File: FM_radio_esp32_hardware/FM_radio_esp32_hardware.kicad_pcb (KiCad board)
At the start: 2 copper layers, 85 x 117 mm, 47 parts, among them J1 AudioJack2_Ground_SwitchT, J2 Conn_01x06, J3 Conn_02x03_Odd_Even, J4 Conn_02x03_Odd_Even, SW1 SW_Push, SW2 SW_SPDT, SW3 SW_SPST, U1 ESP32-WROOM-32D, U2 RDA5807

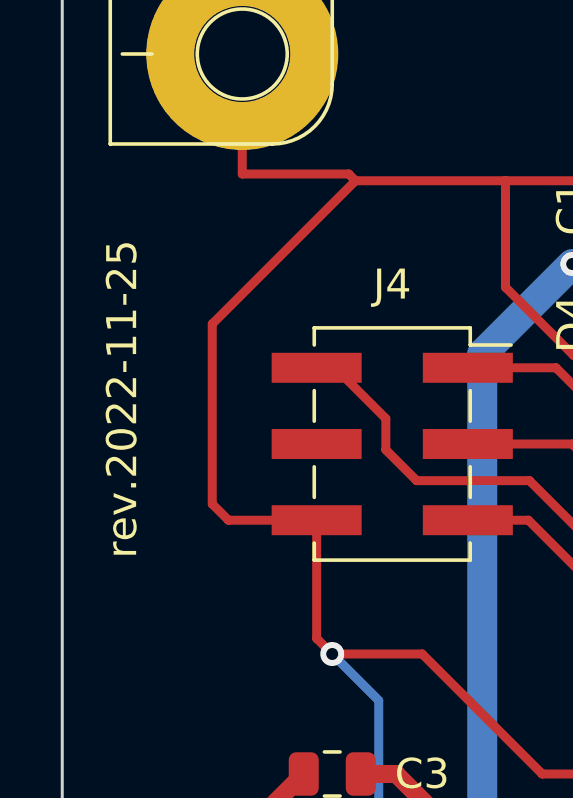
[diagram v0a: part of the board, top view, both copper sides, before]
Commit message: fix a too big silk pattern
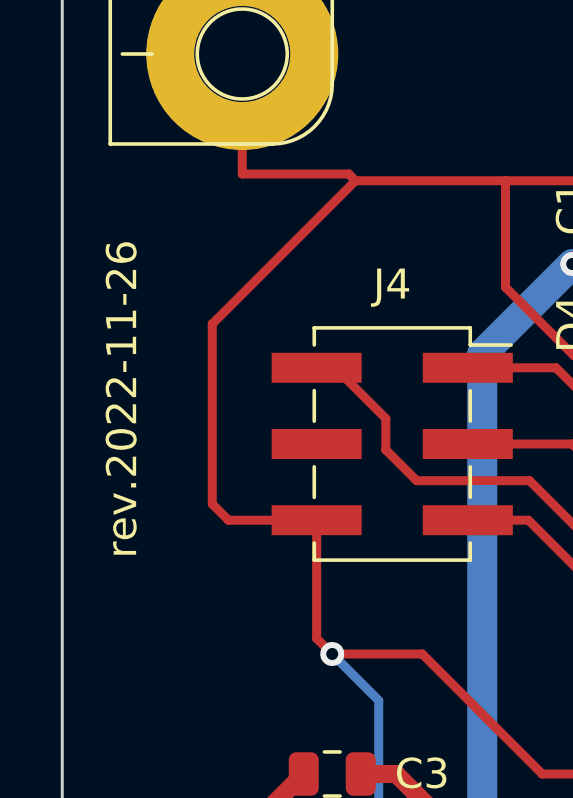
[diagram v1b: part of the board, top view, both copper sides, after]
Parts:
- removed the G*** at (110.0, 56.0)
- added G***: LOGO, FM_radio_esp32:electronics_fig_5_s2, B.Cu at (82.0, 63.0)
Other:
- board text added: "rev.2022-11-26"
- board text removed: "rev.2022-11-25"
